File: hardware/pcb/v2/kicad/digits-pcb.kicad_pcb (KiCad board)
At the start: 2 copper layers, 76.2 x 56.9 mm, 71 parts, among them J1 Conn_02x20_Odd_Even, J3 VIN_BARREL_PIGTAIL, J4 Conn_01x07, J6 Conn_01x02, J7 Screw_Terminal_01x02, J8 Conn_01x04, J9 Conn_01x03, SW1 SW_Push, U1 LM2596S-5, U2 DRV8871DDAR, U3 RP2040, U4 W25Q16JVSSIQ, U5 AMS1117-3.3, U6 TLV320AIC3104IRHBR, U7 XC6206P182MR, Y1 ABM8-272-T3

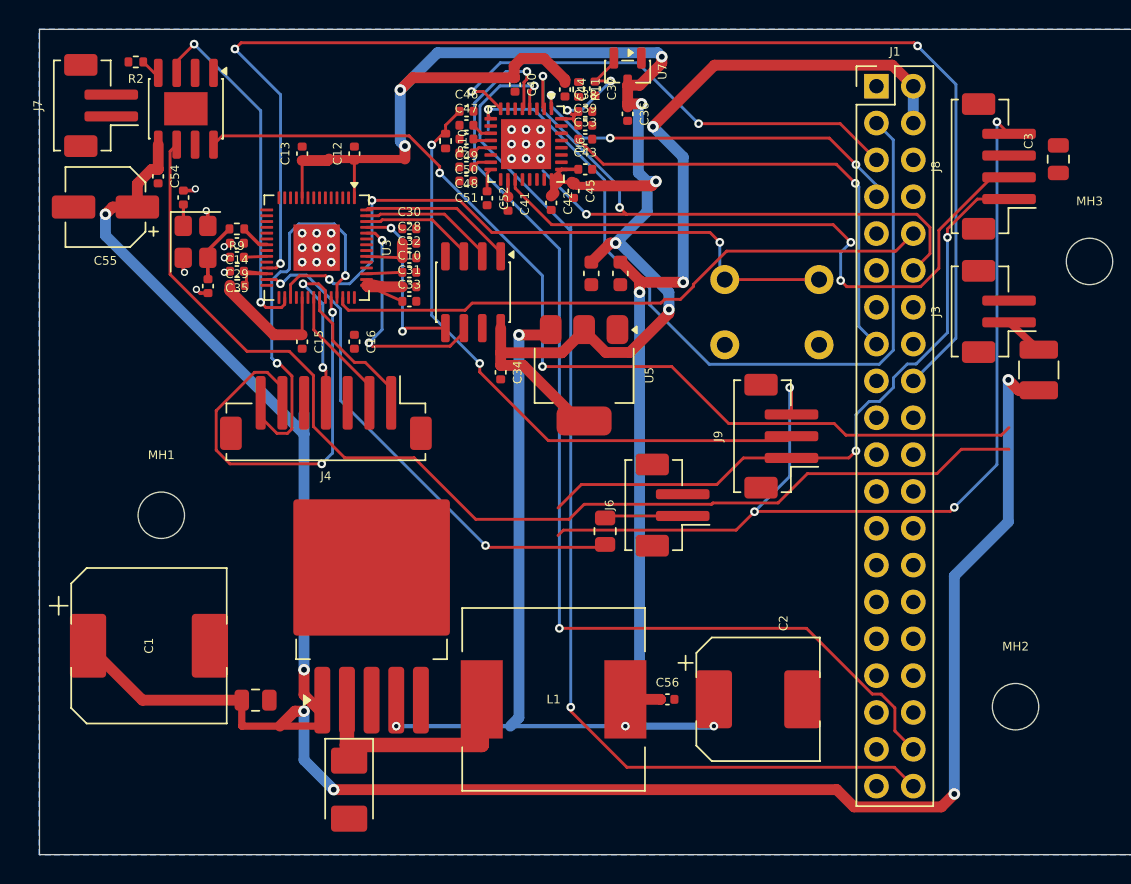
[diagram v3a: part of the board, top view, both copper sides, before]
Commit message: fix(hardware): rip freerouter mess + add 3 more decoupling stubs
Authorized nuke of all unlocked tracks/vias (552 deleted) since the
freerouter mess was getting in the way of the missing decoupling
stubs. Added 3 more locked decoupling stubs via pcbnew script:

  C16->U3.42 (single vertical, no longer blocked by ripped UART_RX_PI)
  C28->U3.49 (3-seg Z route, corner at x=39.5)
  C30->U3.50 (3-seg Z route, corner at x=39.0)

Skipped C14->U3.22: any L-route from C14.1 grazes C29.1 because the
two cap pads are vertically adjacent (~0.97mm apart). Needs manual
fanout via or careful diagonal.

State: 13 of 14 decoupling stubs locked. 0 real DRC violations.
Board has only locked traces now - clean slate for re-routing all
~60 power/signal nets via freerouter or OrthoRoute.
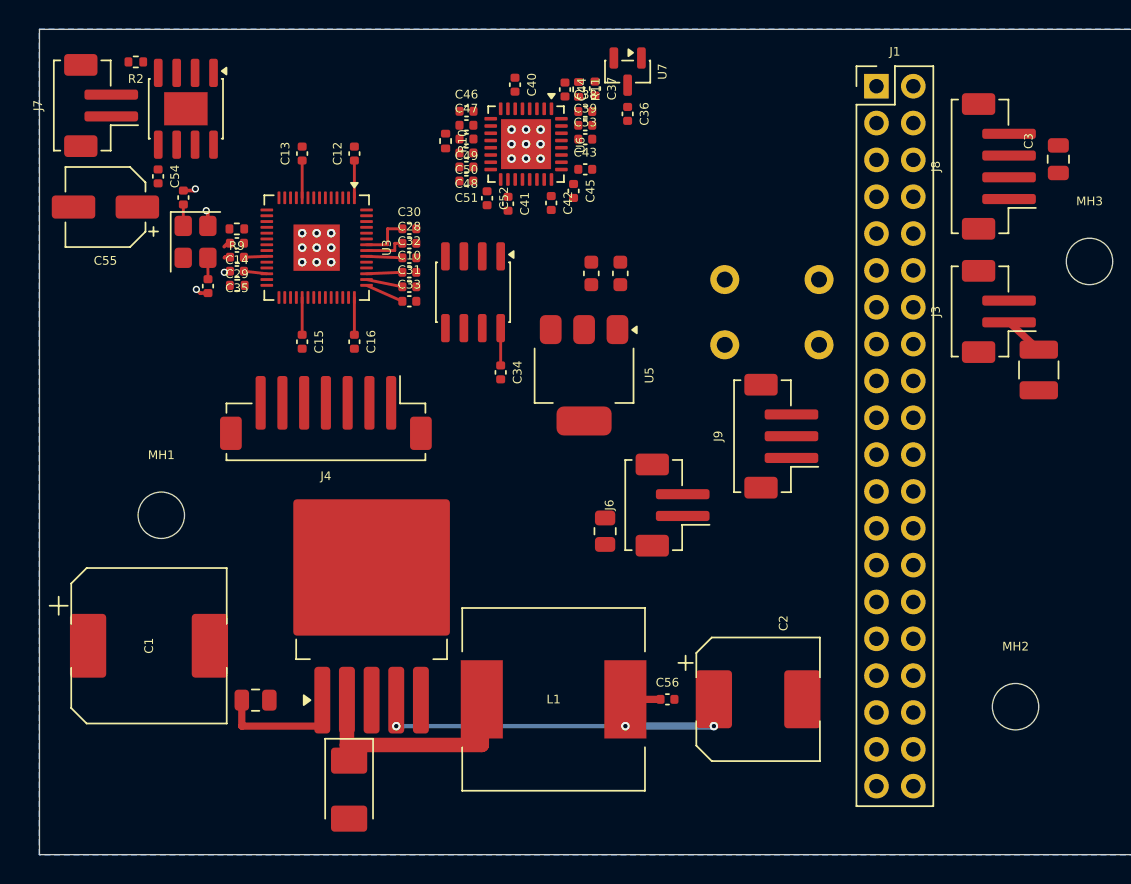
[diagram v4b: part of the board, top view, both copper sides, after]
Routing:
- net +12V: track 155.3 -> 9.13 mm, vias 6 -> 0
- net +3V3: track 135.1 -> 23.5 mm, vias 7 -> 0
- net +5V: track 131.0 -> 29.8 mm, vias 7 -> 3
- net SWD_SWDIO: track 89.9 -> 0.00 mm, vias 3 -> 0
- net BELL_A: track 78.0 -> 0.00 mm
- net CODEC_DIN: track 76.4 -> 0.00 mm, vias 2 -> 0
- net CODEC_DOUT: track 74.7 -> 0.00 mm, vias 2 -> 0
- net MIC_GND: track 68.6 -> 0.00 mm, vias 4 -> 0
- net BELL_B: track 67.8 -> 0.00 mm, vias 2 -> 0
- net CODEC_SDA: track 57.3 -> 0.00 mm, vias 1 -> 0
- net HOOK_SW: track 46.2 -> 0.00 mm, vias 3 -> 0
- net MIC_HOT: track 46.0 -> 0.00 mm, vias 2 -> 0
- net CODEC_BCLK: track 45.9 -> 0.00 mm, vias 3 -> 0
- net EAR_P: track 44.7 -> 0.00 mm, vias 2 -> 0
- net MIC_FROM_SW: track 43.8 -> 0.00 mm, vias 2 -> 0
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
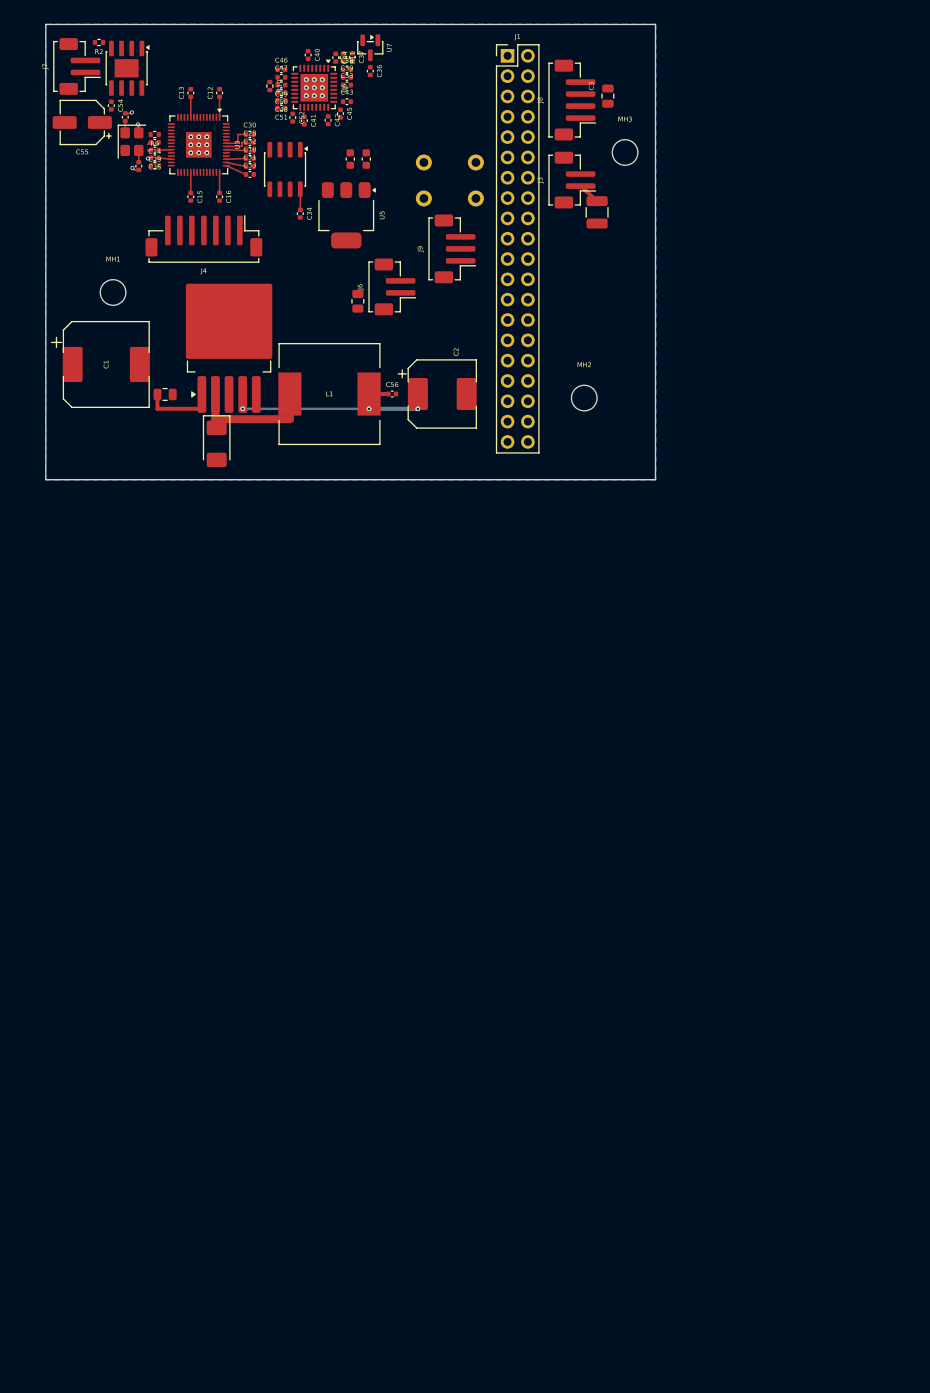
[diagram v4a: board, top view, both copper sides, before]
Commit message: feat(hardware): cluster groups, F.Cu pours, JLC-safe relaxed clearances
- Group all 71 footprints into cluster_buck/ldo/mcu/codec/ringer/mech
- Add F.Cu GND zone (clone of B.Cu) and F.Cu +3V3 pour over U3 cluster
- Use solid pad-to-zone connection on +3V3 pour (lower inductance for decoupling)
- Add 4 EP thermal vias under U3 (0.5mm OD / 0.3mm drill)
- Relax Power+Default netclass clearance to 0.13mm for QFN escape, vias to 0.5/0.3
- Tighten board rules to JLCPCB-safe minimums (min via 0.45, hole-to-hole 0.25)
- Lower zone clearance from 0.5mm to 0.15mm
- Bump buck D1 distance budget from 7.0 to 7.5mm to match physical floor
- Rewrite COMPONENTS.md to match schematic source of truth: codec section
  C36-C53/R10-R11/U6/U7, ringer section, drop nonexistent R3/R4/J10
- All 6 cluster placement checkers PASS, 0 real DRC, 0 intra-cluster
  unconnected for buck/ldo/mcu (cross-cluster keypad/audio/Pi nets remain)
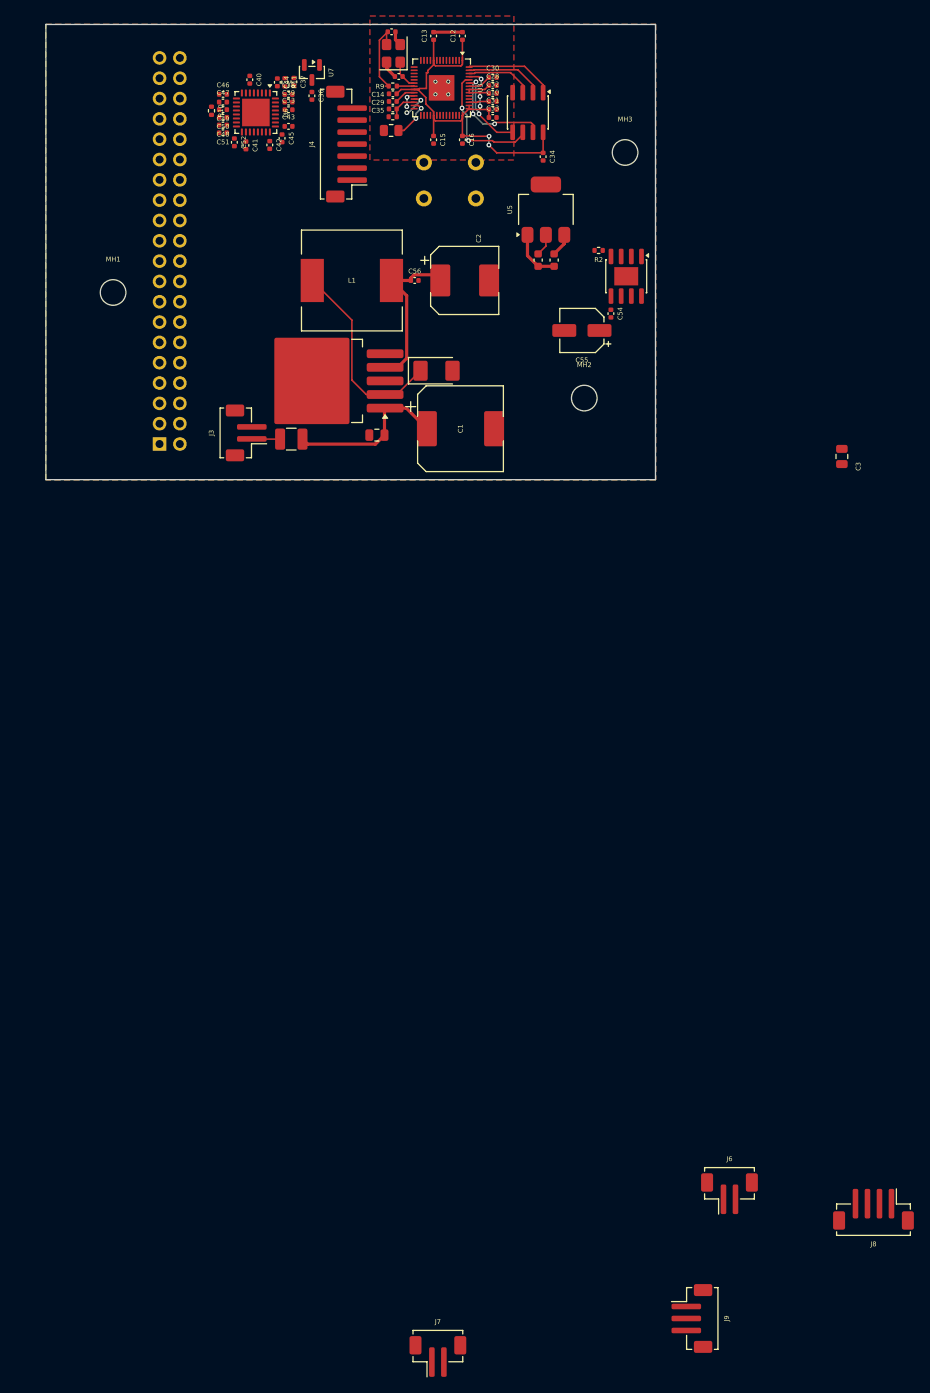
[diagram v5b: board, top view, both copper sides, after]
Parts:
- J1: moved to B.Cu
- moved J7 167.3 mm to (64.0, 181.0), turned to 0 degrees
- moved J8 143.6 mm to (118.5, 162.6), turned to 180 degrees
- moved J9 136.9 mm to (95.8, 176.2), turned to -90 degrees
- moved J6 120.8 mm to (100.5, 160.6), turned to 0 degrees
- moved C54 67.6 mm to (85.6, 50.6)
- moved C55 67.6 mm to (82.0, 52.7)
- moved R2 67.6 mm to (84.1, 42.7)
- moved U2 67.6 mm to (87.5, 45.9)
- moved J1 65.2 mm to (29.2, 66.9)
- moved C3 53.7 mm to (114.5, 68.5), turned to -90 degrees
- moved J3 51.9 mm to (40.0, 65.5)
- moved F1 47.6 mm to (45.7, 66.3), turned to 0 degrees
- moved C1 45.0 mm to (66.8, 65.0)
- moved C6 35.8 mm to (58.2, 15.4), turned to 0 degrees
- moved C5 34.6 mm to (59.1, 21.0), turned to 180 degrees
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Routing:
- net +3V3: track 23.5 -> 62.0 mm, vias 0 -> 4
- net QSPI_SCLK: track 0.00 -> 16.1 mm, vias 0 -> 2
- net QSPI_SD3: track 0.00 -> 14.3 mm, vias 0 -> 3
- net QSPI_SD0: track 0.00 -> 12.0 mm, vias 0 -> 2
- net +12V: track 9.13 -> 20.7 mm
- net QSPI_SS: track 0.00 -> 11.2 mm
- net GND: track 4.19 -> 14.1 mm, vias 22 -> 4
- net QSPI_SD1: track 0.00 -> 9.76 mm
- net QSPI_SD2: track 0.00 -> 8.37 mm
- net XOUT: track 1.47 -> 9.79 mm
- net SW_NODE: track 16.8 -> 25.1 mm
- net +5V: track 29.8 -> 23.5 mm, vias 3 -> 0
- net LED_OUT: track 0.00 -> 5.38 mm, vias 0 -> 2
- net SWD_SWDIO: track 0.00 -> 3.31 mm, vias 0 -> 2
- net XIN: track 1.48 -> 3.70 mm
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- added copper zone on F.Cu, net +3V3
- added copper zone on F.Cu, net GND

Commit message: feat(hardware): codec cluster placement + J4 keypad routing checkpoint
- Place codec cluster (U6/U7/C36-C53/R10/R11) with all 20 placement
  constraints PASS
- Route J4 keypad fanout: 7 KP_COL/KP_ROW signals from U3 south edge to
  J4 east column with B.Cu via crossings for the zigzag mismatch
- Relax mic frontend budgets in codec_targets.json: C46/C47/C48 (AC
  coupling/MICBIAS bypass) 2.0->3.0mm, R10 (MICBIAS series) 4.0->6.0mm.
  Rationale: TLV320AIC3104 datasheet SLAS510G section 13.1 only mandates
  tight placement for power-supply decoupling caps, not coupling caps or
  series resistors. Speech-band signals at ~10kOhm impedance are
  insensitive to sub-mm trace length variations.
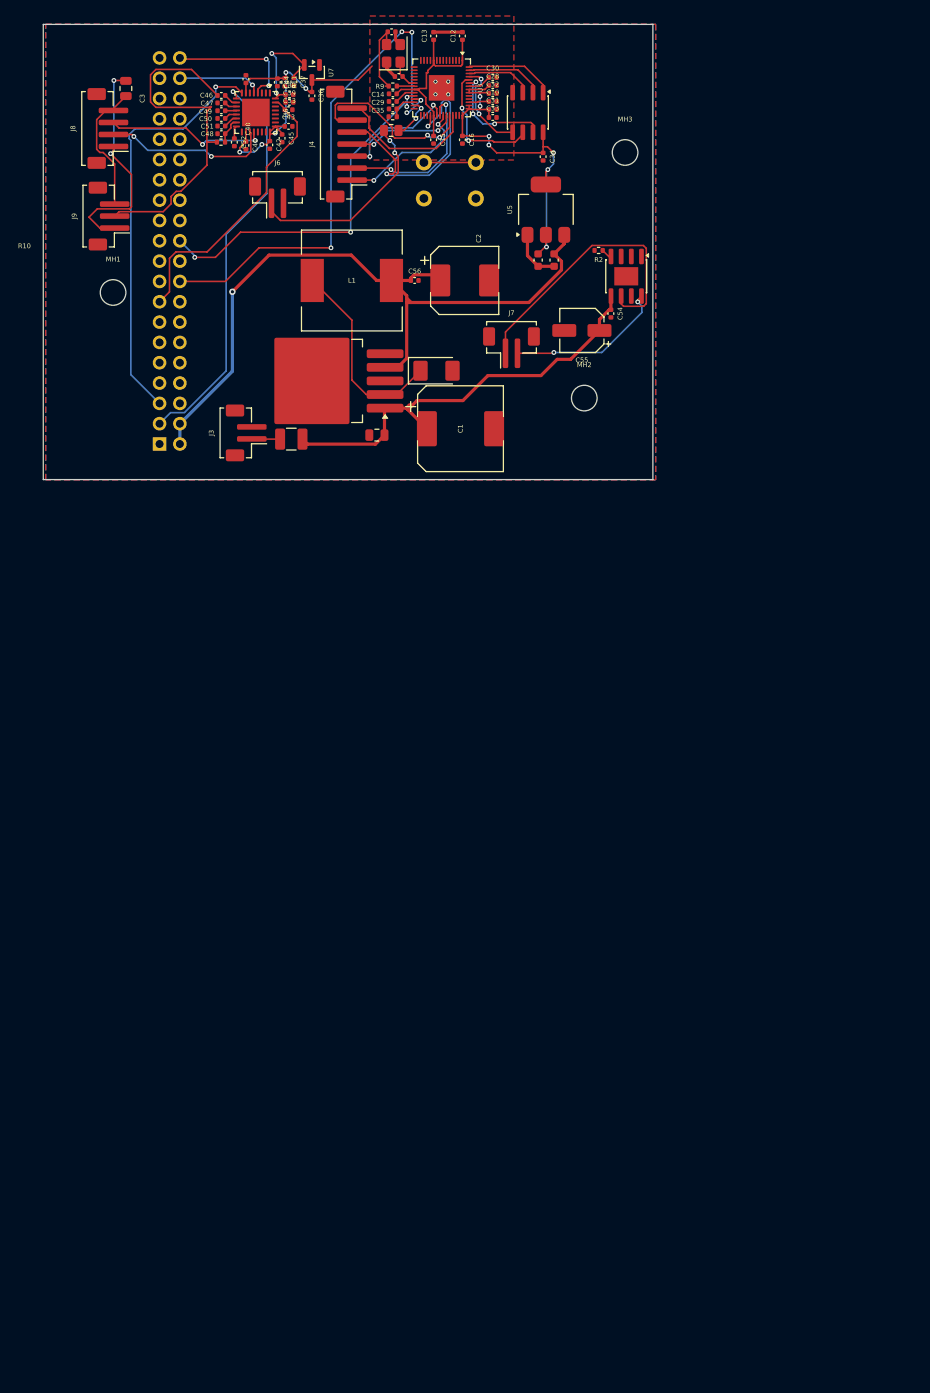
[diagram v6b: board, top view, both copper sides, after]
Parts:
- moved J8 165.6 mm to (22.8, 27.5), turned to 90 degrees
- moved J9 155.9 mm to (22.9, 38.4), turned to 90 degrees
- moved J6 136.7 mm to (44.0, 36.1)
- moved J7 126.4 mm to (73.2, 54.9)
- moved C3 100.6 mm to (25.0, 22.5)
- moved R10 4.10 mm to (36.9, 29.2), turned to 0 degrees
- moved C48 1.10 mm to (36.9, 28.1)
- moved C51 0.87 mm to (36.9, 27.2)
- moved C40 0.49 mm to (40.0, 21.3), turned to 90 degrees
- moved C46 0.25 mm to (36.9, 23.3)
- moved C49 0.25 mm to (36.9, 25.2)
- moved C50 0.25 mm to (36.9, 26.2)
- moved C47 0.23 mm to (36.9, 24.3)
- moved C39 0.12 mm to (45.4, 24.2)
- moved C38 0.12 mm to (45.4, 23.2)
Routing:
- net +5V: track 23.5 -> 92.5 mm, vias 0 -> 1
- net SWD_SWDIO: track 3.31 -> 65.3 mm, vias 2 -> 5
- net +3V3: track 62.0 -> 116.5 mm, vias 4 -> 12
- net CODEC_SCL: track 0.00 -> 52.7 mm, vias 0 -> 1
- net CODEC_SDA: track 0.00 -> 50.9 mm, vias 0 -> 1
- net MIC_FROM_SW: track 0.00 -> 45.0 mm
- net SWD_SWCLK: track 2.14 -> 45.2 mm, vias 2 -> 4
- net BELL_A: track 0.00 -> 36.2 mm
- net CODEC_RESET: track 0.00 -> 35.7 mm
- net +12V: track 20.7 -> 54.7 mm
- net KP_ROW2: track 0.00 -> 31.5 mm, vias 0 -> 2
- net MIC_HOT: track 0.00 -> 29.2 mm, vias 0 -> 2
- net LED_A: track 0.00 -> 25.8 mm, vias 0 -> 2
- net KP_ROW1: track 0.00 -> 22.9 mm, vias 0 -> 2
- net KP_COL1: track 0.00 -> 21.1 mm, vias 0 -> 2
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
